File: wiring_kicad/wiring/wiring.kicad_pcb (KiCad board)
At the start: 2 copper layers, 120 x 74.9 mm, 23 parts, among them IC1 UA741CP, IC2 UA741CP, J1 Trigger IN, J2 Signal IN, J3 Analog Out, J4 Signal + Analog Out, J5 PJ-202A, U1 Teensy2.0_(Arduino), U2 MCP4725_bkt, U3 L7805CV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

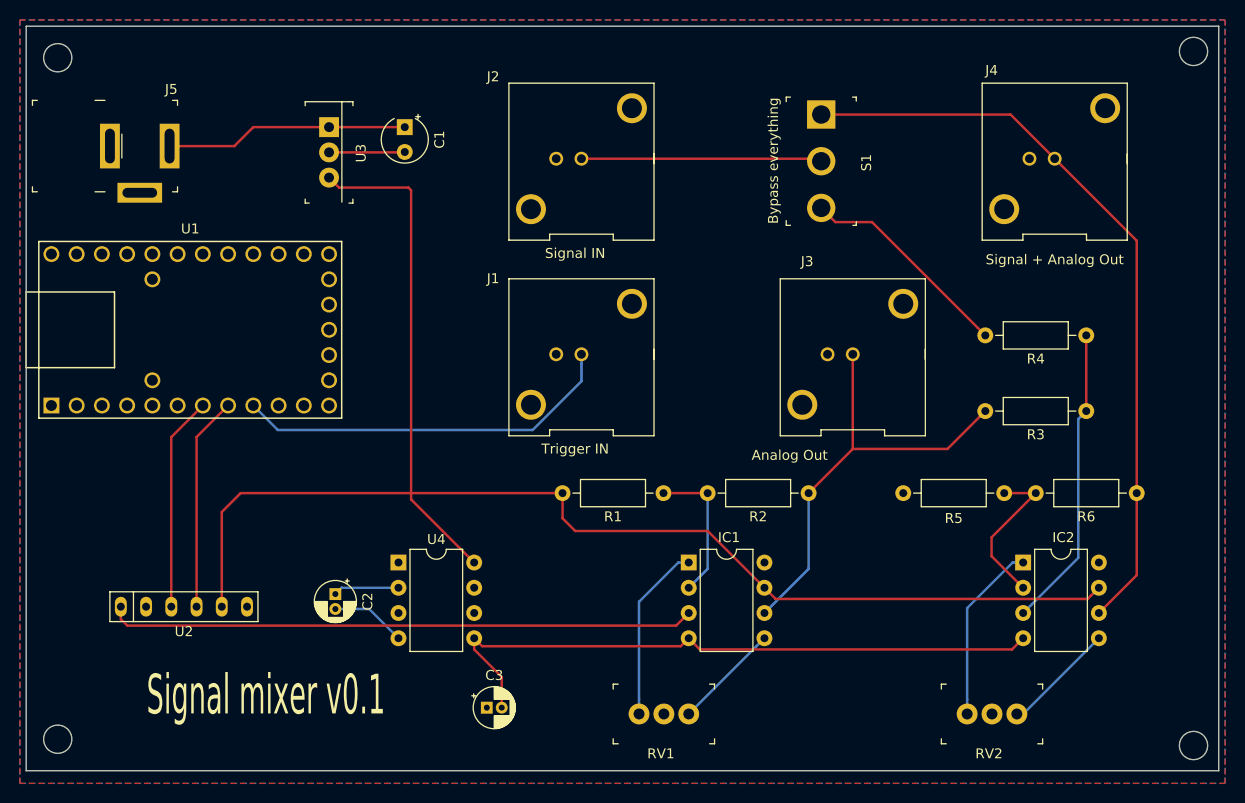
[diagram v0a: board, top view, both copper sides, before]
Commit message: fixed PCB bug, added serial comm to Teensy board
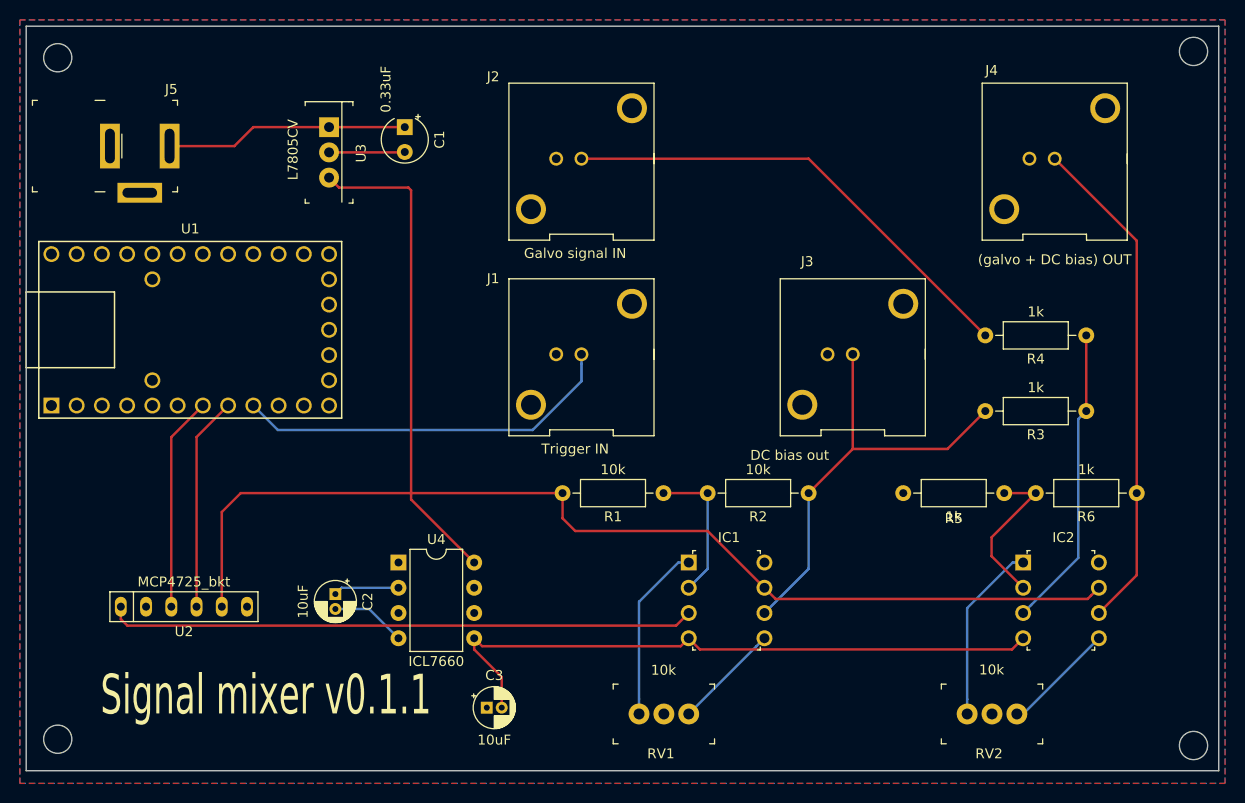
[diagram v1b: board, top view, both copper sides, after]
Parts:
- removed S1: Bypass everything, digikey-footprints:Toggle_Switch_100SP1T1B4M2QE
- IC1, IC2: footprint Package_DIP:DIP-8_W7.62mm -> digikey-footprints:DIP-8_W7.62mm
- J2: value Signal IN -> Galvo signal IN
- J3: value Analog Out -> DC bias out
- J4: value Signal + Analog Out -> (galvo + DC bias) OUT
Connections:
- R4 pad 2: Net-(R4-Pad2) -> Net-(J2-Pad1)
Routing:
- net Net-(IC2-Pad6): track 76.1 -> 50.7 mm
- net Net-(J2-Pad1): track 24.2 -> 48.0 mm
- net Net-(R4-Pad2): track 21.8 -> 0.00 mm
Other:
- board text added: "Signal mixer v0.1.1"
- board text removed: "Signal mixer v0.1"
